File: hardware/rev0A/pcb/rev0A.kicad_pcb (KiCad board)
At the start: 4 copper layers, 100 x 100 mm, 87 parts, among them IC1 ESP32-C3-WROOM-02-H4, IC2 TXS0102DCU, IC3 ADC088S022CIMTX_NOPB, J1 Conn_01x02_Socket, J2 Conn_01x02_Socket, J3 Conn_01x02_Socket, J4 Conn_01x03_Socket, J5 Conn_01x02_Socket, J6 Conn_01x03_Socket, J7 Conn_01x06_Socket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

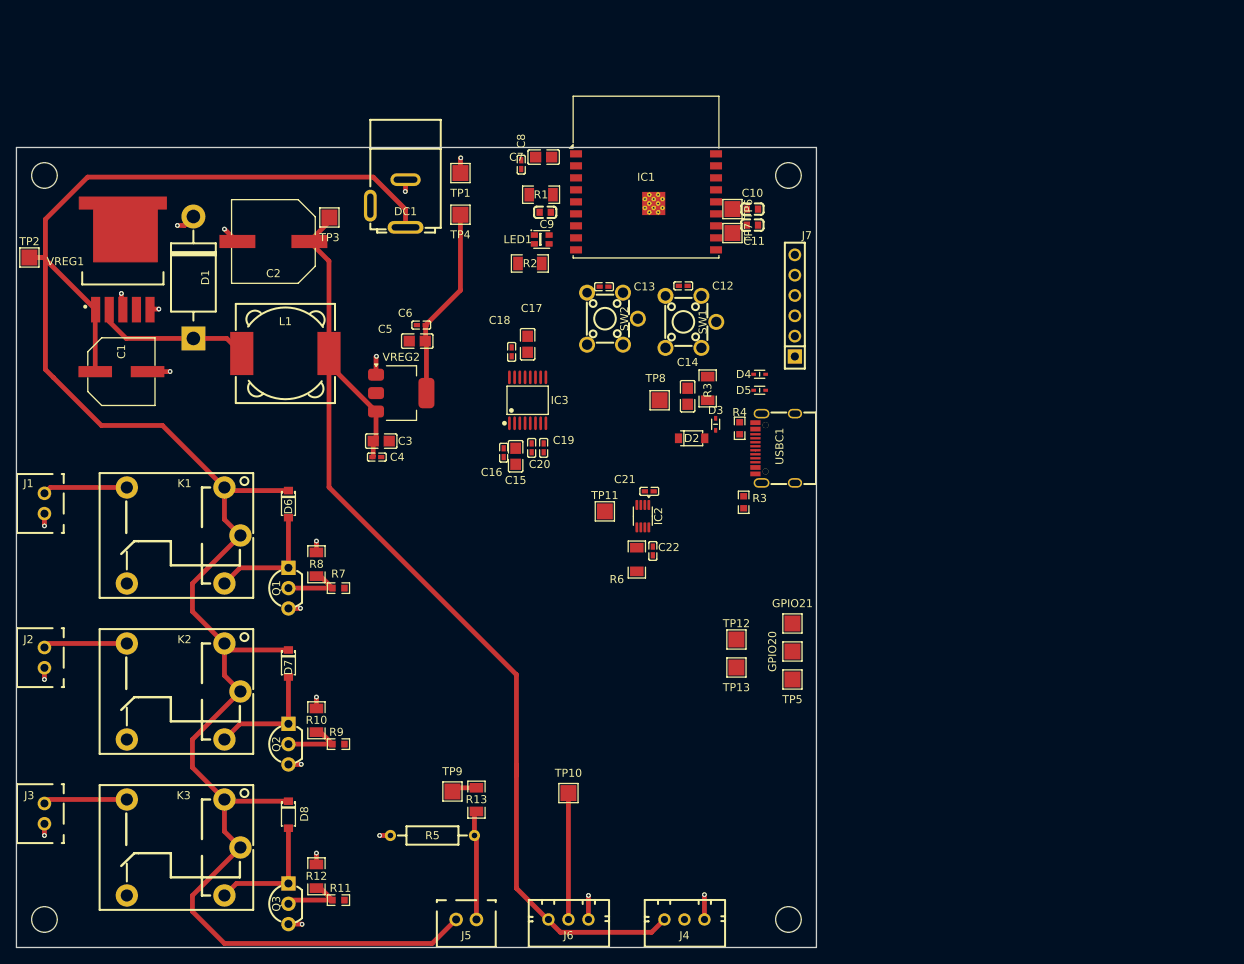
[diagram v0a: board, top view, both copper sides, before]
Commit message: Completes most PCB routing
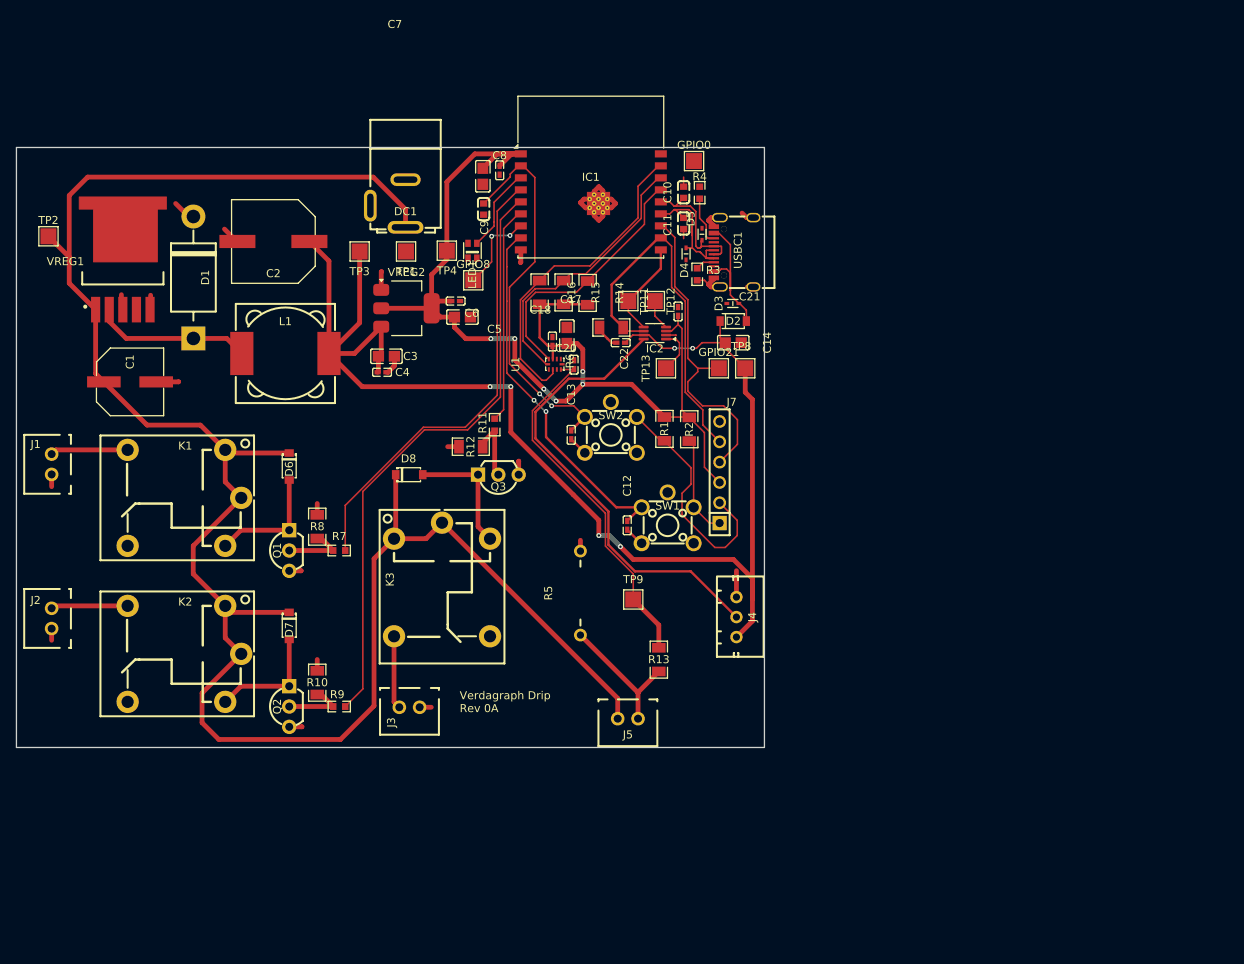
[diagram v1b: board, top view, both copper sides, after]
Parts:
- removed C15: 10uF, easyeda2kicad:C0805
- removed C16, C19: 0.1uF, easyeda2kicad:C0402
- removed GPIO20: ~, TestPoint:TestPoint_Pad_2.0x2.0mm
- removed IC3: ADC088S022CIMTX_NOPB, easyeda2kicad:TSSOP-16_L5.0-W4.4-P0.65-LS6.4-BL
- removed J6: Conn_01x03_Socket, easyeda2kicad:CONN-TH_3P-P2.50_A2501WV2-3P
- removed the R3 at (140.9, 72.1)
- removed REF** (x4): MountingHole_3.2mm_M3, MountingHole:MountingHole_3.2mm_M3
- removed TP10, TP5, TP6, TP7: TestPoint, TestPoint:TestPoint_Pad_2.0x2.0mm
- added GPIO0: ~, TestPoint:TestPoint_Pad_2.0x2.0mm, F.Cu at (139.2, 43.7)
- added GPIO8: ~, TestPoint:TestPoint_Pad_2.0x2.0mm, F.Cu at (111.6, 58.6)
- added R14: 10000, easyeda2kicad:R1206, F.Cu at (125.9, 60.2)
- added R15: 10000, easyeda2kicad:R1206, F.Cu at (122.9, 60.1)
- added R16: 10000, easyeda2kicad:R1206, F.Cu at (119.9, 60.1)
- added U1: ADS1115IRUGT, easyeda2kicad:X2QFN-10_L2.0-W1.5-P0.50-TL_RUG0010B, F.Cu at (121.8, 69.1)
- R5: value 220 -> 120; footprint easyeda2kicad:RES-TH_BD2.3-L6.5-P10.50-D0.5 -> easyeda2kicad:RES-TH_BD2.2-L6.5-P10.50-D0.6
- moved R11 62.6 mm to (114.3, 76.7), turned to -90 degrees
- moved Q3 59.7 mm to (114.7, 82.9), turned to 180 degrees
- moved R12 57.1 mm to (111.3, 79.4), turned to 180 degrees
- moved J3 47.5 mm to (103.6, 112.0), turned to 180 degrees
- moved K3 46.5 mm to (107.7, 96.0), turned to -90 degrees
- moved D8 45.1 mm to (103.6, 82.9), turned to 0 degrees
- moved TP12 43.5 mm to (134.3, 61.2), turned to -90 degrees
- moved TP13 38.4 mm to (135.7, 69.6), turned to -90 degrees
- moved J4 38.4 mm to (144.5, 100.7), turned to 90 degrees
- moved R5 35.5 mm to (125.0, 97.7), turned to 90 degrees
- moved GPIO21 33.2 mm to (142.3, 69.6)
- moved R1 33.1 mm to (135.5, 77.2), turned to -90 degrees
- moved TP9 33.0 mm to (131.6, 98.5)
- moved J5 32.2 mm to (130.9, 113.4)
- moved C12 30.7 mm to (130.8, 89.2), turned to -90 degrees
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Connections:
- net Pressure Sensor (Current) renamed Pressure Sensor Voltage
- C7 pad 2: +3V3 -> +3.3V
- C8 pad 2: +3V3 -> +3.3V
- GPIO21 pad 1: unconnected-(GPIO21-Pad1) -> IO21
- IC1 pad 1: +3V3 -> +3.3V
- IC1 pad 11: IO20 -> Flow Sensor Enable
- IC1 pad 15: ACD Chip Select -> SDA
- IC1 pad 16: SDA -> SCLK
- IC1 pad 17: SCLK -> ADC Alert
- IC1 pad 18: ACD Program -> Net-(IC1-IO0)
- IC1 pad 7: Flow Sensor Enable -> Net-(IC1-IO8)
- J7 pad 3: +3V3 -> +3.3V
- J7 pad 5: IO20 -> Flow Sensor Enable
- R1 pad 1: +3V3 -> +3.3V
- R2 pad 1: +3V3 -> +3.3V
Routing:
- net +3.3V: track 24.3 -> 134.4 mm, vias 0 -> 6
- net CHIP_PU: track 0.00 -> 78.6 mm, vias 0 -> 2
- net Relay2: track 0.00 -> 75.5 mm
- net GPIO9: track 0.00 -> 58.6 mm, vias 0 -> 2
- net Relay1: track 0.00 -> 57.4 mm
- net Net-(IC2-B1): track 0.00 -> 57.4 mm
- net Flow Sensor Enable: track 0.00 -> 46.4 mm
- net Pressure Sensor Voltage: track 3.19 -> 45.2 mm
- net ADC Alert: track 0.00 -> 40.2 mm
- net IO21: track 0.00 -> 39.8 mm
- net +5V: track 133.9 -> 172.0 mm, vias 0 -> 6
- net GND: track 37.5 -> 73.6 mm, vias 20 -> 0
- net SCLK: track 0.00 -> 34.6 mm
- net SDA: track 0.00 -> 32.5 mm
- net Relay3: track 0.00 -> 27.1 mm
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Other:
- board size 100 x 100 mm -> 93.5 x 75 mm
- copper layers 4 -> 2
- board text added: "Verdagraph Drip Rev 0A"

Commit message: Completes PCB and drafts firmware structure
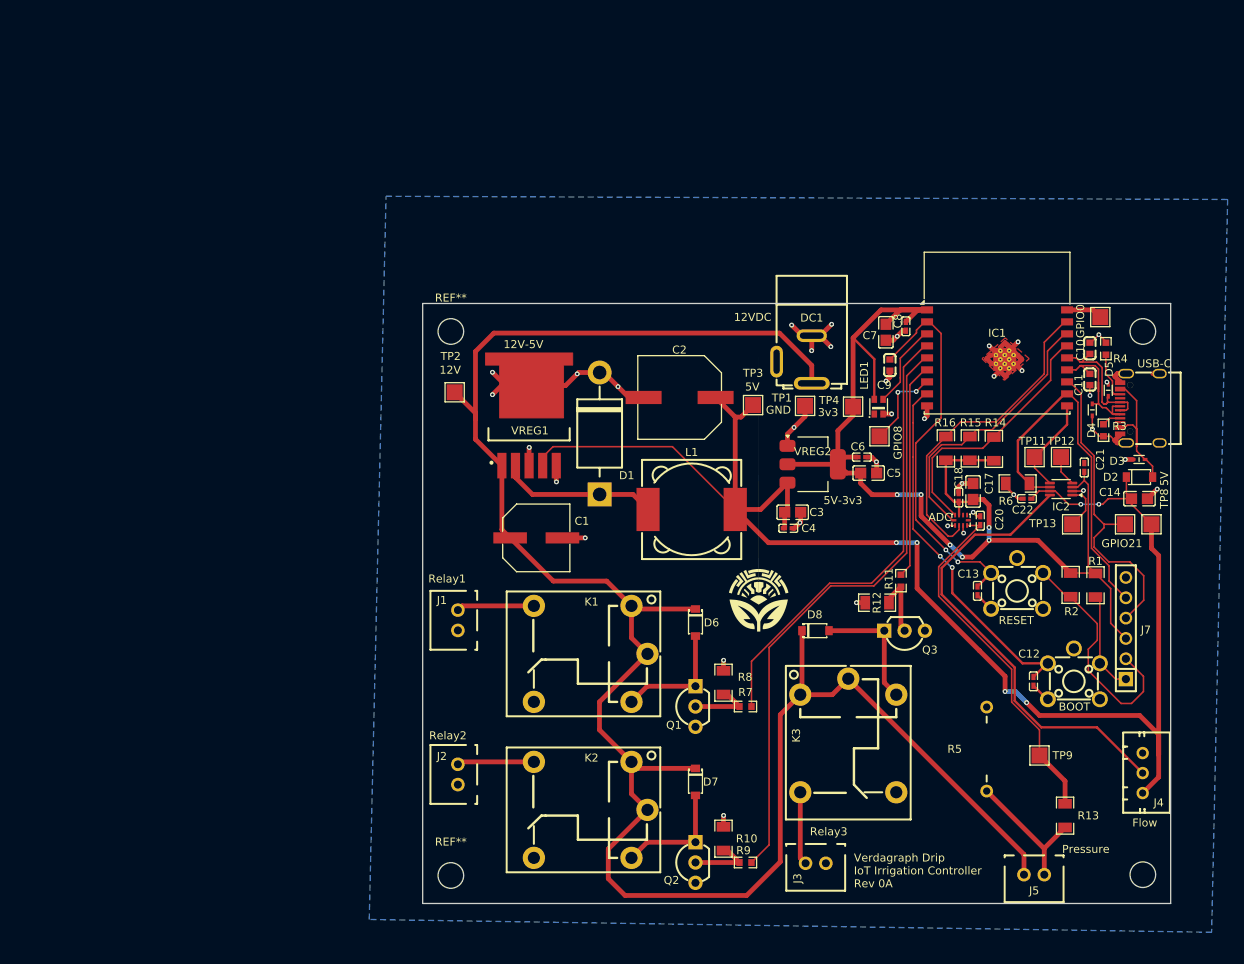
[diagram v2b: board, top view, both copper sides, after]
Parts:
- added G***: LOGO, Drip:logo_small, F.Cu at (147.3, 98.6)
- added REF**: MountingHole_3.2mm_M3, MountingHole:MountingHole_3.2mm_M3, F.Cu at (108.8, 133.0)
- added REF**: MountingHole_3.2mm_M3, MountingHole:MountingHole_3.2mm_M3, F.Cu at (108.8, 65.0)
- added REF**: MountingHole_3.2mm_M3, MountingHole:MountingHole_3.2mm_M3, F.Cu at (195.3, 65.0)
- added REF**: MountingHole_3.2mm_M3, MountingHole:MountingHole_3.2mm_M3, F.Cu at (195.3, 132.9)
- moved C17 54.4 mm to (174.1, 85.0)
- moved IC1 54.4 mm to (177.1, 68.3)
- moved Q3 54.4 mm to (165.5, 102.4)
- moved R12 54.4 mm to (162.1, 98.9)
- moved TP4 54.4 mm to (159.1, 74.4)
- moved U1 54.4 mm to (172.6, 88.6)
- moved J1 54.4 mm to (109.7, 101.1)
- moved J2 54.4 mm to (109.7, 120.4)
- moved C1 54.4 mm to (119.5, 90.8)
- moved C10 54.4 mm to (188.7, 67.1)
- moved C11 54.4 mm to (188.7, 71.0)
- moved C12 54.4 mm to (181.6, 108.7)
- moved C13 54.4 mm to (174.6, 97.4)
- moved C14 54.4 mm to (194.9, 85.9)
- moved C18 54.4 mm to (172.3, 85.8)
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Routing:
- net GND: track 73.6 -> 130.8 mm, vias 0 -> 37
- net +5V: track 172.0 -> 189.4 mm
- net +3.3V: track 134.4 -> 143.6 mm
- net Net-(IC1-IO0): track 0.00 -> 4.52 mm
- added copper zone on B.Cu, net GND
- added copper zone on F.Cu, net GND
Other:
- board text added: "12V"
- board text added: "12V-5V"
- board text added: "12VDC"
- board text added: "3v3"
- board text added: "5V"
- board text added: "5V-3v3"
- board text added: "ADC"
- board text added: "BOOT"
- board text added: "Flow"
- board text added: "GND"
- board text added: "Pressure"
- board text added: "RESET"
- board text added: "Relay1"
- board text added: "Relay2"
- board text added: "Relay3"
- board text added: "USB-C"
- board text added: "Verdagraph Drip IoT Irrigation Controller Rev 0A"
- board text removed: "Verdagraph Drip Rev 0A"

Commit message: PCB needs some final polish, adds structure of FSM and other managers
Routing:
- net D-: track 18.3 -> 17.2 mm
- net GND: track 130.8 -> 130.0 mm
